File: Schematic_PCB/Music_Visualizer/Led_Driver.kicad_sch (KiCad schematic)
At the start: 90 parts, among them U10 LM3915N-1, U11 LM3915N-1, U12 LM3915N-1, U13 LM3915N-1, U14 LM3915N-1, U15 LM3915N-1, U9 LM3915N-1

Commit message: Used Global labels
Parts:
- gave numbers to parts that had none: 4
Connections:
- net Rhi_ref is gone; now on net Rhi_Value: U10.6 (RHI), U11.6 (RHI), U12.6 (RHI), U13.6 (RHI), U14.6 (RHI), U15.6 (RHI), U9.6 (RHI)
- net VBass is gone; now on net VSubBass: U10.5 (SIG)
- net VBrilliance is gone; now on net VSubBass: U15.5 (SIG)
- net VLowerMidrange is gone; now on net VSubBass: U11.5 (SIG)
- net VMidrange is gone; now on net VSubBass: U12.5 (SIG)
- net VPresence is gone; now on net VSubBass: U14.5 (SIG)
- net VUpperMidrange is gone; now on net VSubBass: U13.5 (SIG)
- net Rhi_Value: now reaches U17.3 (-), U17.4
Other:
- note removed: "Rhi_ref"
- moved on the sheet: C57, JP2, RV1

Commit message: Start PCB
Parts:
- D10, D2, D3, D4, D5, D6, D7, D8, D9: value LED -> (none)
- D11, D12, D13, D14, D15, D16, D17, D18, D19, D20, D21, D22, D23, D24, D25, D26, D27, D28, D29, D30, D31, D32, D33, D34, D35, D36, D37, D38, D39, D40, D41, D42, D43, D44, D45, D46, D47, D48, D49, D50, D51, D52, D53, D54, D55, D56, D57, D58, D59, D60, D61, D62, D63, D64, D65, D66, D67, D68, D69, D70: footprint (none) -> LED_THT:LED_D5.0mm
- R76, R77, R78, R79, R80, R81: value 680 -> (none)

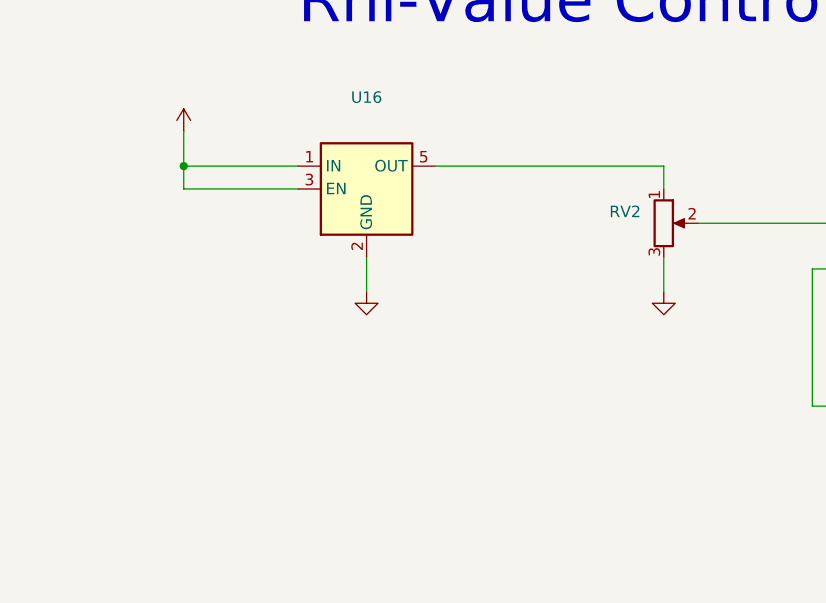
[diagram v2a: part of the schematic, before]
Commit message: Organized all subcircuits in PCB editor
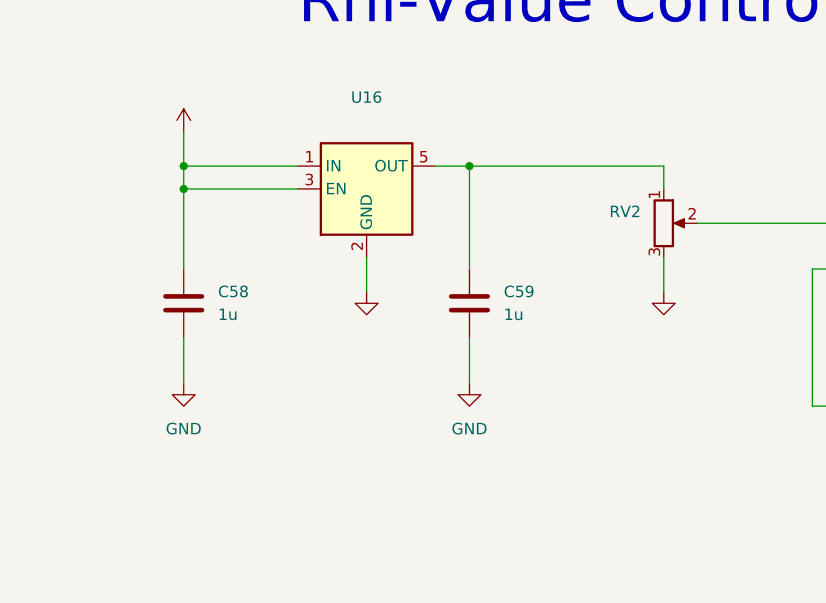
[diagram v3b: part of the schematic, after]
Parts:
- added C58, C59: 1u, Capacitor_SMD:C_0402_1005Metric, symbol Device:C
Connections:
- net +5V: now also C58.1
- net GND: now also C58.2, C59.2
- net at RV2.1, U16.5 (OUT): now also C59.1
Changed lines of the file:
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@@
   (junction (at 64.77 293.37) (diameter 0) (color 0 0 0 0)
   )
+  (junction (at 436.88 209.55) (diameter 0) (color 0 0 0 0)
+  )
   (junction (at 448.31 293.37) (diameter 0) (color 0 0 0 0)
   )
@@
   (junction (at 287.02 294.64) (diameter 0) (color 0 0 0 0)
   )
+  (junction (at 468.63 207.01) (diameter 0) (color 0 0 0 0)
+  )
   (junction (at 261.62 107.95) (diameter 0) (color 0 0 0 0)
   )
@@
     (stroke (width 0) (type default) (color 0 0 0 0))
   )
+  (wire (pts (xy 436.88 226.06) (xy 436.88 231.14))
+    (stroke (width 0) (type default) (color 0 0 0 0))
+  )
   (wire (pts (xy 209.55 45.72) (xy 214.63 45.72))
     (stroke (width 0) (type default) (color 0 0 0 0))
@@
     (stroke (width 0) (type default) (color 0 0 0 0))
   )
+  (wire (pts (xy 468.63 207.01) (xy 490.22 207.01))
+    (stroke (width 0) (type default) (color 0 0 0 0))
+  )
   (wire (pts (xy 62.23 67.31) (xy 88.9 67.31))
     (stroke (width 0) (type default) (color 0 0 0 0))
@@
     (stroke (width 0) (type default) (color 0 0 0 0))
   )
+  (wire (pts (xy 436.88 209.55) (xy 436.88 218.44))
+    (stroke (width 0) (type default) (color 0 0 0 0))
+  )
   (wire (pts (xy 433.07 363.22) (xy 433.07 359.41))
     (stroke (width 0) (type default) (color 0 0 0 0))
@@
     (stroke (width 0) (type default) (color 0 0 0 0))
   )
-  (wire (pts (xy 464.82 207.01) (xy 490.22 207.01))
+  (wire (pts (xy 464.82 207.01) (xy 468.63 207.01))
     (stroke (width 0) (type default) (color 0 0 0 0))
   )
@@
     (stroke (width 0) (type default) (color 0 0 0 0))
   )
+  (wire (pts (xy 468.63 207.01) (xy 468.63 218.44))
+    (stroke (width 0) (type default) (color 0 0 0 0))
+  )
   (wire (pts (xy 227.33 209.55) (xy 227.33 220.98))
     (stroke (width 0) (type default) (color 0 0 0 0))
@@
     (stroke (width 0) (type default) (color 0 0 0 0))
   )
+  (wire (pts (xy 468.63 226.06) (xy 468.63 231.14))
+    (stroke (width 0) (type default) (color 0 0 0 0))
+  )
   (wire (pts (xy 105.41 200.66) (xy 127 200.66))
     (stroke (width 0) (type default) (color 0 0 0 0))
@@
     (pin "1")
   )
+  (symbol (lib_id "Device:C") (at 436.88 222.25 0) (unit 1)
+    (in_bom yes) (on_board yes) (fields_autoplaced)
+    (property "Reference" "C58" (id 0) (at 440.69 220.9799 0)
+      (effects (font (size 1.27 1.27)) (justify left))
+    )
+    (property "Value" "1u" (id 1) (at 440.69 223.5199 0)
+      (effects (font (size 1.27 1.27)) (justify left))
+    )
+    (property "Footprint" "Capacitor_SMD:C_0402_1005Metric" (id 2) (at 437.8452 226.06 0)
+      (effects (font (size 1.27 1.27)) hide)
+    )
+    (property "Datasheet" "https://www.mouser.ca/datasheet/2/212/1/C0603X102K4RACAUTO-2933386.pdf" (id 3) (at 436.88 222.25 0)
+      (effects (font (size 1.27 1.27)) hide)
+    )
+    (pin "1")
+    (pin "2")
+  )
   (symbol (lib_id "Device:LED") (at 480.06 53.34 90) (unit 1)
     (in_bom yes) (on_board yes) (fields_autoplaced)
@@
     (pin "2")
   )
+  (symbol (lib_id "Device:C") (at 468.63 222.25 0) (unit 1)
+    (in_bom yes) (on_board yes) (fields_autoplaced)
+    (property "Reference" "C59" (id 0) (at 472.44 220.9799 0)
+      (effects (font (size 1.27 1.27)) (justify left))
+    )
+    (property "Value" "1u" (id 1) (at 472.44 223.5199 0)
+      (effects (font (size 1.27 1.27)) (justify left))
+    )
+    (property "Footprint" "Capacitor_SMD:C_0402_1005Metric" (id 2) (at 469.5952 226.06 0)
+      (effects (font (size 1.27 1.27)) hide)
+    )
+    (property "Datasheet" "https://www.mouser.ca/datasheet/2/212/1/C0603X102K4RACAUTO-2933386.pdf" (id 3) (at 468.63 222.25 0)
+      (effects (font (size 1.27 1.27)) hide)
+    )
+    (pin "1")
+    (pin "2")
+  )
   (symbol (lib_id "power:+9V") (at 196.85 45.72 0) (unit 1)
     (in_bom yes) (on_board yes) (fields_autoplaced)
@@
     (pin "2")
   )
+  (symbol (lib_id "power:GND") (at 468.63 231.14 0) (unit 1)
+    (in_bom yes) (on_board yes) (fields_autoplaced)
+    (property "Reference" "#PWR?" (id 0) (at 468.63 237.49 0)
+      (effects (font (size 1.27 1.27)) hide)
+    )
+    (property "Value" "GND" (id 1) (at 468.63 236.22 0))
+    (property "Footprint" "" (id 2) (at 468.63 231.14 0)
+      (effects (font (size 1.27 1.27)) hide)
+    )
+    (property "Datasheet" "" (id 3) (at 468.63 231.14 0)
+      (effects (font (size 1.27 1.27)) hide)
+    )
+    (pin "1")
+  )
   (symbol (lib_id "LM3915_LED_Driver:LM3915N-1") (at 259.08 87.63 90) (unit 1)
     (in_bom yes) (on_board yes) (fields_autoplaced)
@@
     (pin "2")
   )
+  (symbol (lib_id "power:GND") (at 436.88 231.14 0) (unit 1)
+    (in_bom yes) (on_board yes) (fields_autoplaced)
+    (property "Reference" "#PWR?" (id 0) (at 436.88 237.49 0)
+      (effects (font (size 1.27 1.27)) hide)
+    )
+    (property "Value" "GND" (id 1) (at 436.88 236.22 0))
+    (property "Footprint" "" (id 2) (at 436.88 231.14 0)
+      (effects (font (size 1.27 1.27)) hide)
+    )
+    (property "Datasheet" "" (id 3) (at 436.88 231.14 0)
+      (effects (font (size 1.27 1.27)) hide)
+    )
+    (pin "1")
+  )
   (symbol (lib_id "Device:LED") (at 43.18 185.42 90) (unit 1)

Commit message: Sourced on_off switch and added on_off switch/indicator circuit
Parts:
- D1, D10, D2, D3, D4, D5, D6, D7, D8, D9: value (none) -> LED; footprint (none) -> LED_THT:LED_D5.0mm
- JP2: value (none) -> Jumper_2_Open; footprint (none) -> Connector_PinHeader_2.54mm:PinHeader_2x01_P2.54mm_Vertical
- R75, R76, R77, R78, R79, R80, R81: value (none) -> 680; footprint (none) -> Resistor_SMD:R_0603_1608Metric
- RV1: value (none) -> 5k_LED_Brightness_Pot; footprint (none) -> Potentiometer_THT:Potentiometer_Bourns_PTV09A-1_Single_Vertical
- RV2: value (none) -> 5k_Rhi_Adjuster; footprint (none) -> Potentiometer_THT:Potentiometer_Bourns_PTV09A-1_Single_Vertical
- U16: value (none) -> NCP161ASN350T1G; footprint (none) -> Package_TO_SOT_SMD:SOT-23-5
- U17: value (none) -> NCS333ASQ3T2G; footprint (none) -> Package_TO_SOT_SMD:SOT-353_SC-70-5

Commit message: Got 3D models for all parts, corrected signal voltage to each driver and made outline of PCB
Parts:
- RV1: value 5k_LED_Brightness_Pot -> (none); footprint Potentiometer_THT:Potentiometer_Bourns_PTV09A-1_Single_Vertical -> (none)
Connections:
- net GND: now also RV2.1; no longer RV2.3
- net VSubBass: no longer U10.5 (SIG), U11.5 (SIG), U12.5 (SIG), U13.5 (SIG), U14.5 (SIG), U15.5 (SIG)
- net at C59.1, U16.5 (OUT): now also RV2.3; no longer RV2.1
- new net VBass: U10.5 (SIG)
- new net VBrilliance: U15.5 (SIG)
- new net VLowerMidrange: U11.5 (SIG)
- new net VMidrange: U12.5 (SIG)
- new net VPresence: U14.5 (SIG)
- new net VUpperMidrange: U13.5 (SIG)

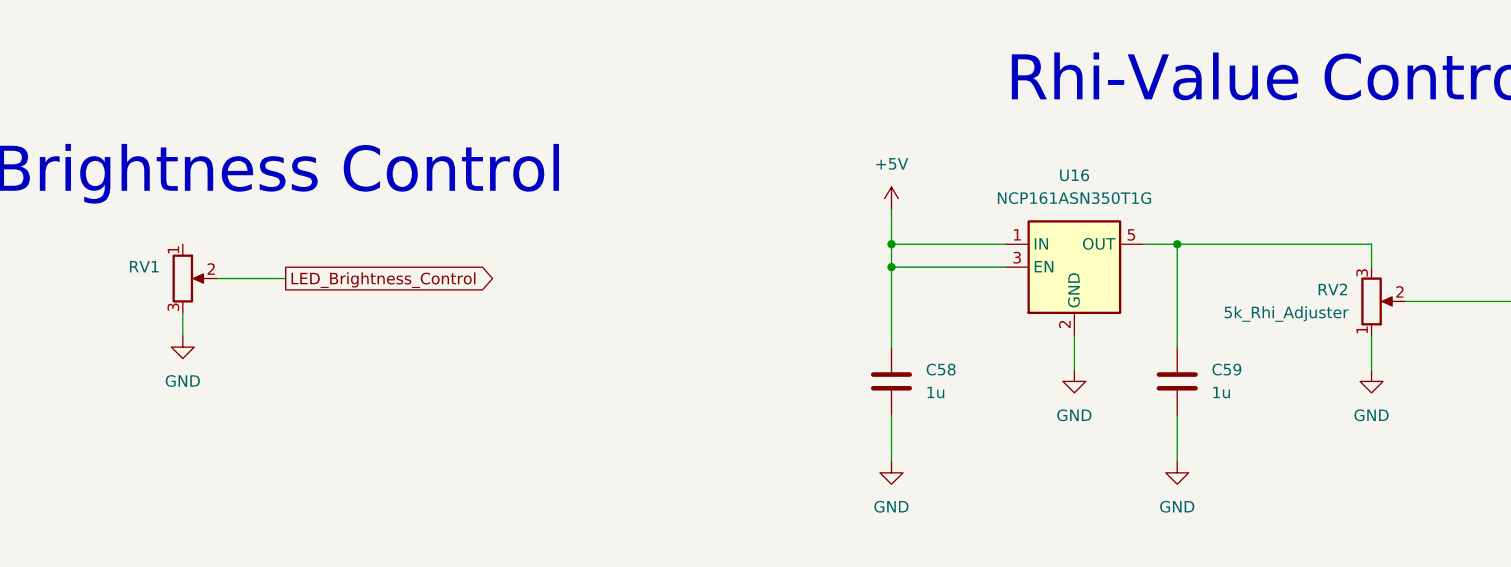
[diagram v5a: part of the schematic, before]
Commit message: Both parts ar PVT09A 5K ohms, corrected footprint terminal labels
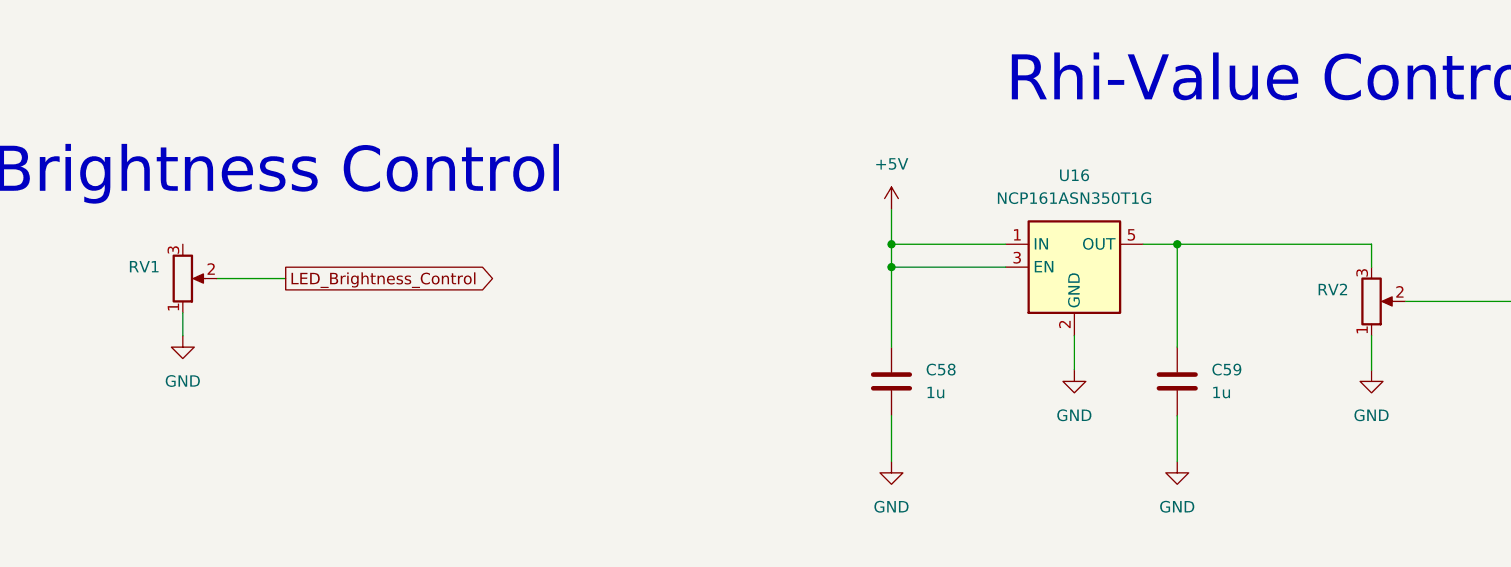
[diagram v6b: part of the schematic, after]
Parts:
- RV2: value 5k_Rhi_Adjuster -> (none); footprint Potentiometer_THT:Potentiometer_Bourns_PTV09A-1_Single_Vertical -> (none)
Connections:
- net GND: now also RV1.1; no longer RV1.3
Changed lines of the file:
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@@
     (pin "2")
   )
-  (symbol (lib_id "Device:R_Potentiometer") (at 358.14 210.82 0) (unit 1)
+  (symbol (lib_id "Device:R_Potentiometer") (at 358.14 210.82 0) (mirror x) (unit 1)
     (in_bom yes) (on_board yes) (fields_autoplaced)
     (property "Reference" "RV1" (id 0) (at 355.6 209.5499 0)
@@
       (effects (font (size 1.27 1.27)) (justify right))
     )
-    (property "Value" "5k_Rhi_Adjuster" (id 1) (at 487.68 214.6299 0)
+    (property "Value" "" (id 1) (at 487.68 214.6299 0)
       (effects (font (size 1.27 1.27)) (justify right))
     )
-    (property "Footprint" "Potentiometer_THT:Potentiometer_Bourns_PTV09A-1_Single_Vertical" (id 2) (at 490.22 213.36 0)
+    (property "Footprint" "" (id 2) (at 490.22 213.36 0)
       (effects (font (size 1.27 1.27)) hide)
     )

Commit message: Added 10 uF polarized smoothing capacitors to LED driver ciruit
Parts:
- removed C57: 220u, Capacitor_THT:CP_Radial_D6.3mm_P2.50mm, symbol Device:C_Polarized
- added C59: (no value), symbol Device:C_Polarized
- added C60, C61, C62, C63, C64, C65: 10u, Capacitor_THT:CP_Radial_D5.0mm_P2.00mm, symbol Device:C_Polarized
- RV1: value (none) -> 10k_LED_Brightness_Pot; footprint (none) -> PTV09A_Pot_Vertical:PTV09
- RV2: value (none) -> 5k_Rhi_Adjuster; footprint (none) -> PTV09A_Pot_Vertical:PTV09
- renumbered C58 to C57, C59 to C58
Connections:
- net +9V: now also C59.1, C60.1, C61.1, C62.1, C63.1, C64.1, C65.1
- net GND: now also C59.2, C60.2, C61.2, C62.2, C63.2, C64.2, C65.2

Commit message: Added 7th LM324 Quad-op-amp IC to Filter array, updated numbering on all other ICs
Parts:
- removed C60, C61, C62, C63, C64, C65: 10u, Capacitor_THT:CP_Radial_D5.0mm_P2.00mm, symbol Device:C_Polarized
- C59: value (none) -> 10u; footprint (none) -> Capacitor_THT:CP_Radial_D5.0mm_P2.00mm
- renumbered U9 to U10, U10 to U11, U11 to U12, U12 to U13, U13 to U14, U14 to U15, U15 to U16, U16 to U17, U17 to U18
